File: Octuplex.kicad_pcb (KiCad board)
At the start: 2 copper layers, 140 x 140 mm, 21 parts, among them U1 MC68B09, U11 74LS138, U2 MC68B40, U3 MC68B50, U4 27128, U5 HM62256BLP, U6 74LS139, U8 74LS259, X1 CXO_DIP8, X2 CXO_DIP8

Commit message: Break up schematic into hierarchial sheets.
Connect sheets with address and data buses. TODO: add control bus.
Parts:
- added C1: 0.1uF, Capacitor_THT:C_Radial_D6.3mm_H5.0mm_P2.50mm, F.Cu at (232.7, 93.0)
- added C2: 0.1uF, Capacitor_THT:C_Radial_D6.3mm_H5.0mm_P2.50mm, F.Cu at (232.7, 100.8)
- U10: value ~ -> R6522
- U3: value MC68B50 -> MXS6551; footprint Package_DIP:DIP-24_W15.24mm -> Package_DIP:DIP-28_W15.24mm
- U7: value ~ -> MC68B50; footprint Package_DIP:DIP-28_W15.24mm -> Package_DIP:DIP-24_W15.24mm
- moved U10 216.8 mm to (231.6, 19.2), turned to 0 degrees
- moved H2 207.3 mm to (234.0, 85.1)
- moved H1 202.2 mm to (234.0, 77.1)
- moved H3 197.3 mm to (241.9, 77.1)
- moved H8 193.4 mm to (257.8, 85.1)
- moved U7 191.7 mm to (268.4, 19.2), turned to 0 degrees
- moved X1 182.6 mm to (209.6, 50.0)
- moved U8 180.8 mm to (268.4, 51.3), turned to 0 degrees
- moved U11 170.7 mm to (218.8, 19.2)
- moved U6 150.5 mm to (207.9, 19.2)
- moved H4 145.8 mm to (241.9, 85.1)
- moved U9 141.6 mm to (189.5, 19.2)
- moved H7 139.8 mm to (257.8, 77.1)
- moved U1 127.8 mm to (171.1, 19.2)
- moved X2 126.2 mm to (251.7, 65.2)
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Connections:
- U1 pad 2: unconnected-(U1-~{NMI}-Pad2) -> /Microprocessor/~{NMI}
- U1 pad 24: unconnected-(U1-D7-Pad24) -> /d7
- U1 pad 25: unconnected-(U1-D6-Pad25) -> /d6
- U1 pad 26: unconnected-(U1-D5-Pad26) -> /d5
- U1 pad 27: unconnected-(U1-D4-Pad27) -> /d4
- U1 pad 28: unconnected-(U1-D3-Pad28) -> /d3
- U1 pad 29: unconnected-(U1-D2-Pad29) -> /d2
- U1 pad 3: /~{IRQ} -> /Microprocessor/~{IRQ}
- U1 pad 30: unconnected-(U1-D1-Pad30) -> /d1
- U1 pad 31: unconnected-(U1-D0-Pad31) -> /d0
- U1 pad 34: /E -> /Microprocessor/E
- U1 pad 37: /~{RESET} -> /Microprocessor/~{RESET}
- U10 pad 1: unconnected-(U10-VSS-Pad1) -> GND
- U10 pad 20: unconnected-(U10-VCC-Pad20) -> VCC
- U10 pad 21: /~{IRQ} -> /GPIO/~{IRQ}
- U10 pad 25: /E -> /GPIO/E
- U10 pad 34: /~{RESET} -> /GPIO/~{RESET}
- U11 pad 16: unconnected-(U11-VCC-Pad16) -> VCC
- U11 pad 8: unconnected-(U11-GND-Pad8) -> GND
- U2 pad 17: /E -> /Microprocessor/E
- U2 pad 8: /~{RESET} -> /Microprocessor/~{RESET}
- U2 pad 9: /~{IRQ} -> /Microprocessor/~{IRQ}
- U3 pad 1: unconnected-(U3-VSS-Pad1) -> GND
- U3 pad 13: unconnected-(U3-R/~{W}-Pad13) -> /a0
- U3 pad 14: unconnected-(U3-E-Pad14) -> /a1
- U3 pad 15: /d7 -> VCC
- U3 pad 16: /d6 -> unconnected-(U3-~{DCD}-Pad16)
- U3 pad 17: /d5 -> unconnected-(U3-~{DSR}-Pad17)
- U3 pad 18: /d4 -> /d0
- U3 pad 19: /d3 -> /d1
- U3 pad 21: /d1 -> /d3
- U3 pad 22: /d0 -> /d4
- U3 pad 23: unconnected-(U3-~{DCD}-Pad23) -> /d5
- U3 pad 24: unconnected-(U3-~{CTS}-Pad24) -> /d6
- U3 pad 4: unconnected-(U3-Tx_CLK-Pad4) -> /GPIO/~{RESET}
- U3 pad 7: /~{IRQ} -> unconnected-(U3-XTAL2-Pad7)
- U4 pad 22: unconnected-(U4-~{OE}-Pad22) -> /Microprocessor/E
- U7 pad 11: unconnected-(U7-~{DTR}-Pad11) -> /a0
- U7 pad 12: unconnected-(U7-Rx_Data-Pad12) -> VCC
- U7 pad 14: unconnected-(U7-RS1-Pad14) -> /GPIO/E
- U7 pad 15: VCC -> /d7
- U7 pad 16: unconnected-(U7-~{DCD}-Pad16) -> /d6
- U7 pad 17: unconnected-(U7-~{DSR}-Pad17) -> /d5
- U7 pad 18: /d0 -> /d4
- U7 pad 19: /d1 -> /d3
- U7 pad 21: /d3 -> /d1
- U7 pad 22: /d4 -> /d0
- U7 pad 23: /d5 -> unconnected-(U7-~{DCD}-Pad23)
- U7 pad 24: /d6 -> unconnected-(U7-~{CTS}-Pad24)
- U7 pad 4: /~{RESET} -> unconnected-(U7-Tx_CLK-Pad4)
- U7 pad 7: unconnected-(U7-XTAL2-Pad7) -> /GPIO/~{IRQ}
- U8 pad 15: /~{RESET} -> /GPIO/~{RESET}
- U8 pad 16: unconnected-(U8-VCC-Pad16) -> VCC
- U8 pad 8: unconnected-(U8-GND-Pad8) -> GND
- U9 pad 39: /E -> /Microprocessor/E
- U9 pad 4: /~{IRQ} -> /Microprocessor/~{IRQ}
- U9 pad 40: /~{RESET} -> /Microprocessor/~{RESET}
- U9 pad 6: unconnected-(U9-~{NMI}-Pad6) -> /Microprocessor/~{NMI}
- X1 pad 4: unconnected-(X1-GND-Pad4) -> GND
- X1 pad 8: unconnected-(X1-Vcc-Pad8) -> VCC
- X2 pad 4: unconnected-(X2-GND-Pad4) -> GND
- X2 pad 8: unconnected-(X2-Vcc-Pad8) -> VCC

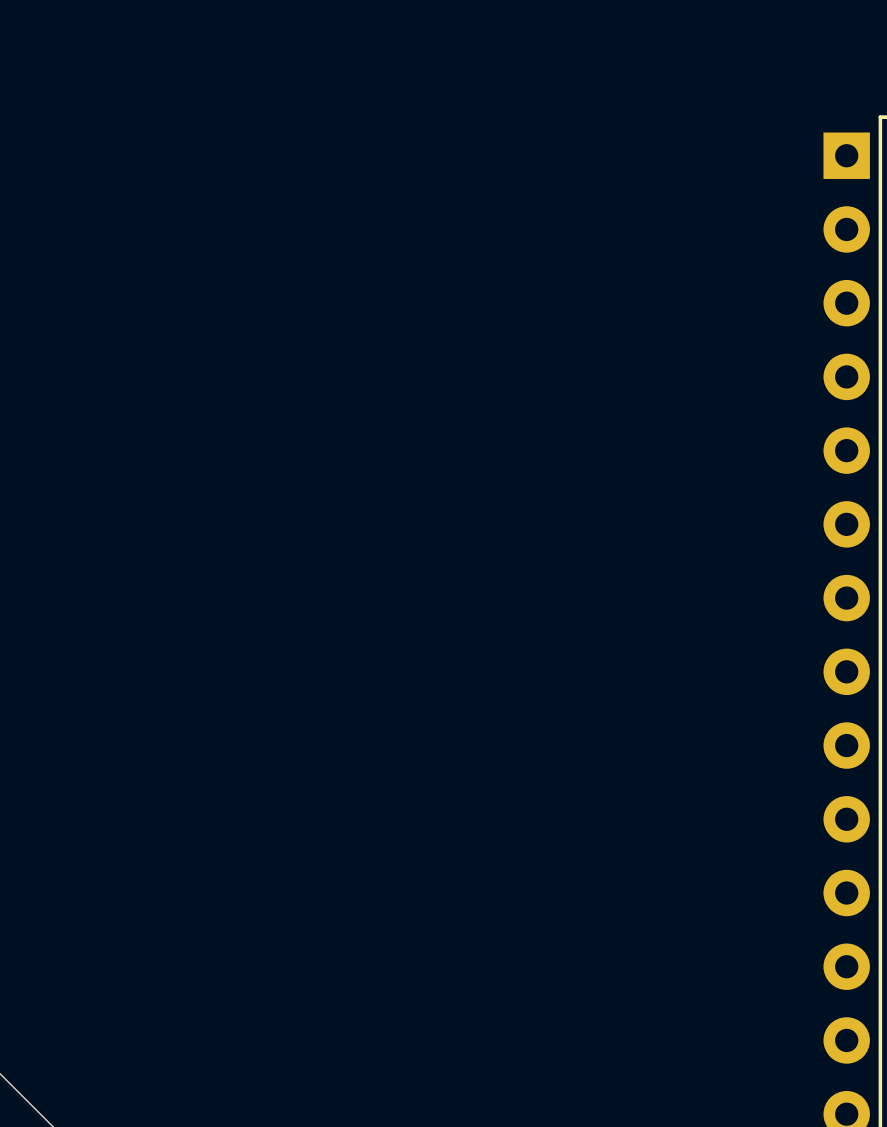
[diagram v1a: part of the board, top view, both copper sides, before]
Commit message: Update schematic.
Pull-up resistors for 6809 signals. 74LS251 mux for 8 input pins. MIDI optoisolator. Wire up 74LS139 for RD and WR. Still many unconnected pins. TODO: connect sheets with control bus.
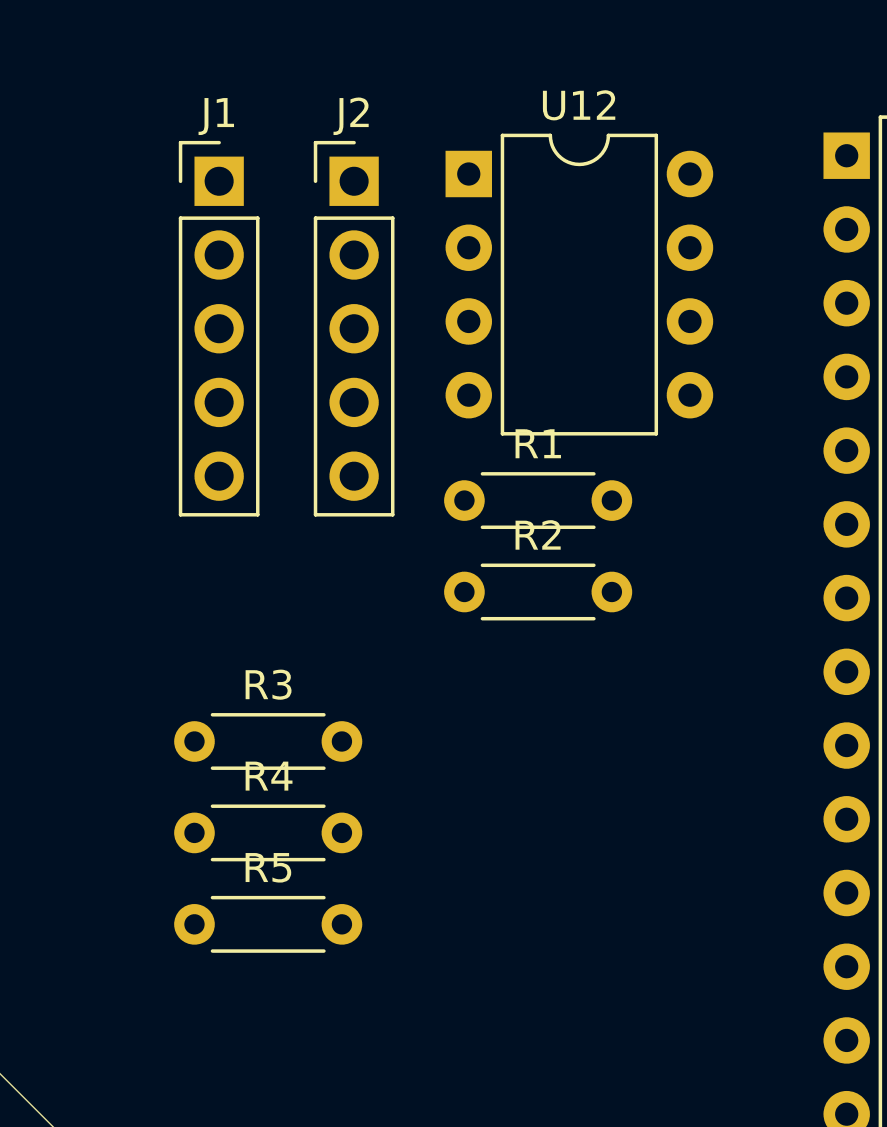
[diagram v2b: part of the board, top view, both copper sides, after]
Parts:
- added J1: DIN-5_180degree, Connector_PinHeader_2.54mm:PinHeader_1x05_P2.54mm_Vertical, F.Cu at (149.4, 20.1)
- added J2: DIN-5_180degree, Connector_PinHeader_2.54mm:PinHeader_1x05_P2.54mm_Vertical, F.Cu at (154.1, 20.1)
- added R1: 220, Resistor_THT:R_Axial_DIN0204_L3.6mm_D1.6mm_P5.08mm_Horizontal, F.Cu at (157.9, 31.1)
- added R2: 280, Resistor_THT:R_Axial_DIN0204_L3.6mm_D1.6mm_P5.08mm_Horizontal, F.Cu at (157.9, 34.3)
- added R3: R, Resistor_THT:R_Axial_DIN0204_L3.6mm_D1.6mm_P5.08mm_Horizontal, F.Cu at (148.6, 39.4)
- added R4: R, Resistor_THT:R_Axial_DIN0204_L3.6mm_D1.6mm_P5.08mm_Horizontal, F.Cu at (148.6, 42.6)
- added R5: R, Resistor_THT:R_Axial_DIN0204_L3.6mm_D1.6mm_P5.08mm_Horizontal, F.Cu at (148.6, 45.7)
- added U12: HCPL-2631, Package_DIP:DIP-8_W7.62mm, F.Cu at (158.0, 19.9)
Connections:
- U1 pad 4: unconnected-(U1-~{FIRQ}-Pad4) -> /Microprocessor/FIRQ
- U10 pad 22: unconnected-(U10-R/~{W}-Pad22) -> /GPIO/R/~{W}
- U10 pad 23: unconnected-(U10-~{CS2}-Pad23) -> /GPIO/~{VIACS}
- U10 pad 24: unconnected-(U10-CS1-Pad24) -> VCC
- U3 pad 28: unconnected-(U3-R/~{W}-Pad28) -> /GPIO/R/~{W}
- U7 pad 10: unconnected-(U7-CS1-Pad10) -> VCC
- U7 pad 2: unconnected-(U7-Rx_Data-Pad2) -> Net-(U12-VO1)
- U7 pad 8: unconnected-(U7-CS0-Pad8) -> VCC
- U7 pad 9: unconnected-(U7-CS2-Pad9) -> /GPIO/~{MIDICS}

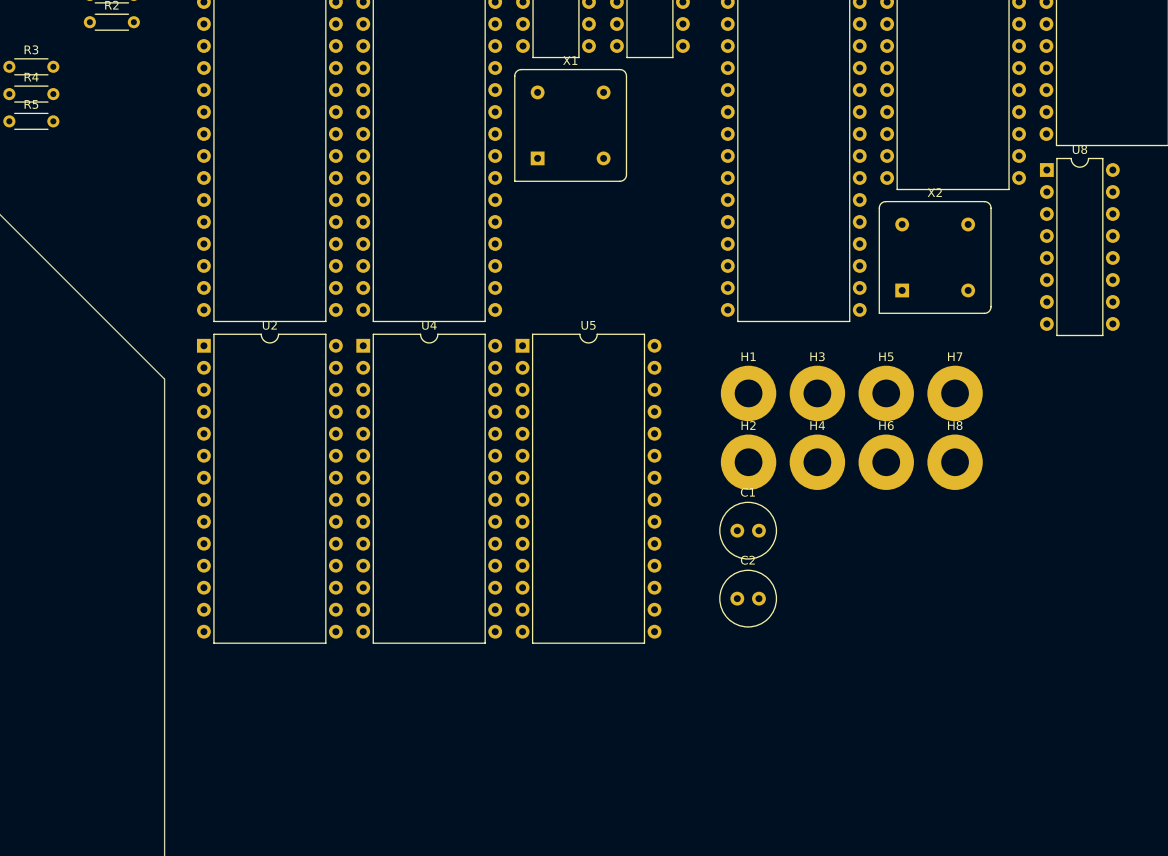
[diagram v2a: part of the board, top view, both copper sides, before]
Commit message: Add control bus.
R/W, E, RD, WR signals from microprocessor to GPIO.
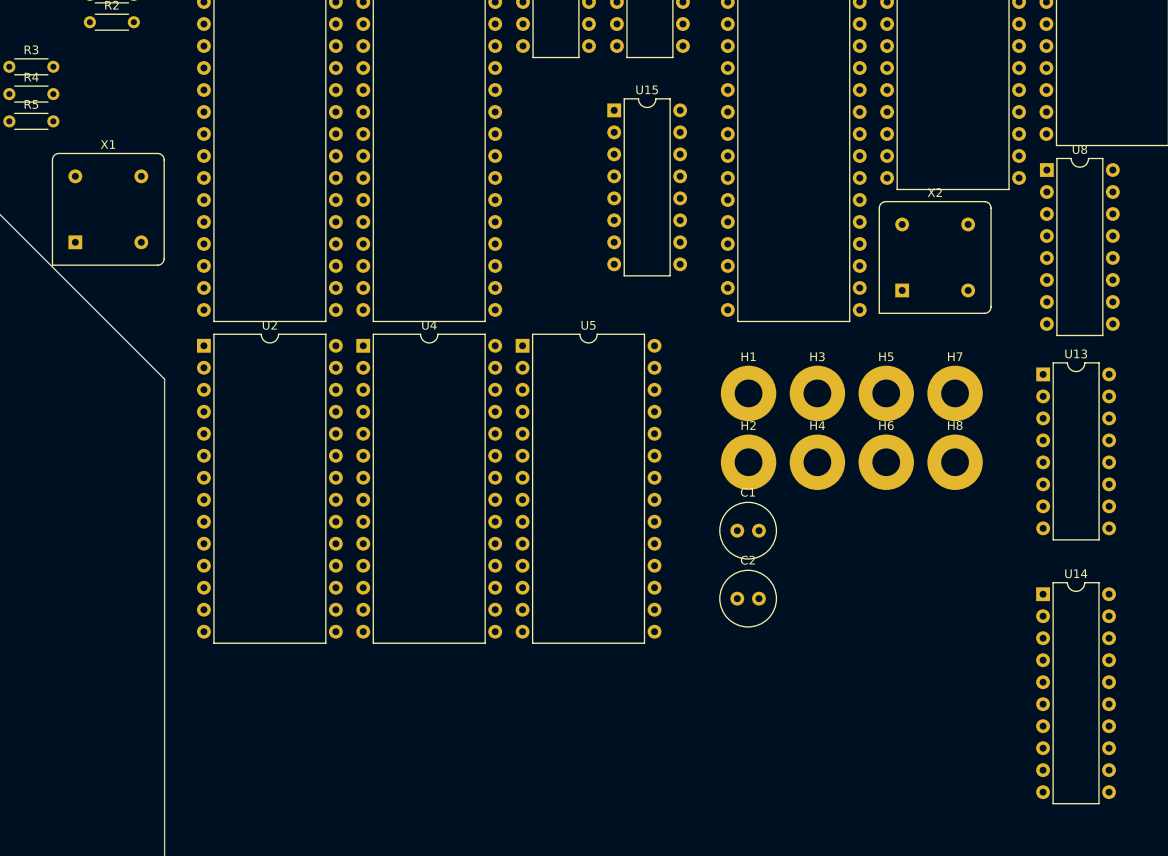
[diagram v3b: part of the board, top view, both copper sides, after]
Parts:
- added U13: 74LS251, Package_DIP:DIP-16_W7.62mm, F.Cu at (268.0, 74.9)
- added U14: PCF8584, Package_DIP:DIP-20_W7.62mm, F.Cu at (268.0, 100.3)
- added U15: 74LS138, Package_DIP:DIP-16_W7.62mm, F.Cu at (218.4, 44.5)
- moved X1 54.3 mm to (156.2, 59.7)
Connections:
- U1 pad 2: /Microprocessor/~{NMI} -> /~{NMI}
- U1 pad 3: /Microprocessor/~{IRQ} -> /~{IRQ}
- U1 pad 32: unconnected-(U1-R/~{W}-Pad32) -> /R/~{W}
- U1 pad 33: unconnected-(U1-~{DMA/BREQ}-Pad33) -> Net-(U1-~{DMA/BREQ})
- U1 pad 34: /Microprocessor/E -> /E
- U1 pad 36: unconnected-(U1-MRDY-Pad36) -> Net-(U1-MRDY)
- U1 pad 37: /Microprocessor/~{RESET} -> /~{RESET}
- U1 pad 38: unconnected-(U1-EXTAL-Pad38) -> Net-(U1-EXTAL)
- U1 pad 4: /Microprocessor/FIRQ -> /~{FIRQ}
- U1 pad 40: unconnected-(U1-~{HALT}-Pad40) -> Net-(U1-~{HALT})
- U10 pad 21: /GPIO/~{IRQ} -> /~{IRQ}
- U10 pad 22: /GPIO/R/~{W} -> /R/~{W}
- U10 pad 25: /GPIO/E -> /E
- U10 pad 34: /GPIO/~{RESET} -> /~{RESET}
- U11 pad 1: unconnected-(U11-A0-Pad1) -> /R/~{W}
- U11 pad 2: unconnected-(U11-A1-Pad2) -> /a11
- U11 pad 3: unconnected-(U11-A2-Pad3) -> /a12
- U11 pad 4: unconnected-(U11-E1-Pad4) -> /Microprocessor/~{IOSEL}
- U11 pad 5: unconnected-(U11-E2-Pad5) -> /a13
- U11 pad 6: /a15 -> /E
- U2 pad 13: unconnected-(U2-R/~{W}-Pad13) -> /R/~{W}
- U2 pad 15: unconnected-(U2-~{CS0}-Pad15) -> /Microprocessor/~{TIMERCS}
- U2 pad 16: unconnected-(U2-CS1-Pad16) -> VCC
- U2 pad 17: /Microprocessor/E -> /E
- U2 pad 8: /Microprocessor/~{RESET} -> /~{RESET}
- U2 pad 9: /Microprocessor/~{IRQ} -> /~{IRQ}
- U3 pad 26: /GPIO/~{IRQ} -> /~{IRQ}
- U3 pad 27: /GPIO/E -> /E
- U3 pad 28: /GPIO/R/~{W} -> /R/~{W}
- U3 pad 4: /GPIO/~{RESET} -> /~{RESET}
- U4 pad 20: unconnected-(U4-~{CE}-Pad20) -> /Microprocessor/~{ROMCS}
- U4 pad 22: /Microprocessor/E -> /~{RD}
- U5 pad 20: unconnected-(U5-~{CS}-Pad20) -> /a15
- U5 pad 22: unconnected-(U5-~{OE}-Pad22) -> /~{RD}
- U5 pad 27: unconnected-(U5-~{WE}-Pad27) -> /~{WR}
- U6 pad 10: unconnected-(U6B-O2-Pad10) -> /Microprocessor/~{IOSEL}
- U6 pad 13: unconnected-(U6B-A1-Pad13) -> /a15
- U6 pad 14: unconnected-(U6B-A0-Pad14) -> /a14
- U6 pad 15: unconnected-(U6B-E-Pad15) -> GND
- U6 pad 2: unconnected-(U6A-A0-Pad2) -> /R/~{W}
- U6 pad 3: unconnected-(U6A-A1-Pad3) -> /E
- U6 pad 6: unconnected-(U6A-O2-Pad6) -> /~{WR}
- U6 pad 7: unconnected-(U6A-O3-Pad7) -> /~{RD}
- U6 pad 9: unconnected-(U6B-O3-Pad9) -> /Microprocessor/~{ROMCS}
- U7 pad 13: unconnected-(U7-R/~{W}-Pad13) -> /R/~{W}
- U7 pad 14: /GPIO/E -> /E
- U7 pad 7: /GPIO/~{IRQ} -> /~{IRQ}
- U8 pad 14: unconnected-(U8-E-Pad14) -> /~{WR}
- U8 pad 15: /GPIO/~{RESET} -> /~{RESET}
- U9 pad 34: unconnected-(U9-R/~{W}-Pad34) -> /R/~{W}
- U9 pad 39: /Microprocessor/E -> /E
- U9 pad 4: /Microprocessor/~{IRQ} -> /~{IRQ}
- U9 pad 40: /Microprocessor/~{RESET} -> /~{RESET}
- U9 pad 6: /Microprocessor/~{NMI} -> /~{NMI}
- X1 pad 5: unconnected-(X1-OUT-Pad5) -> Net-(U1-EXTAL)

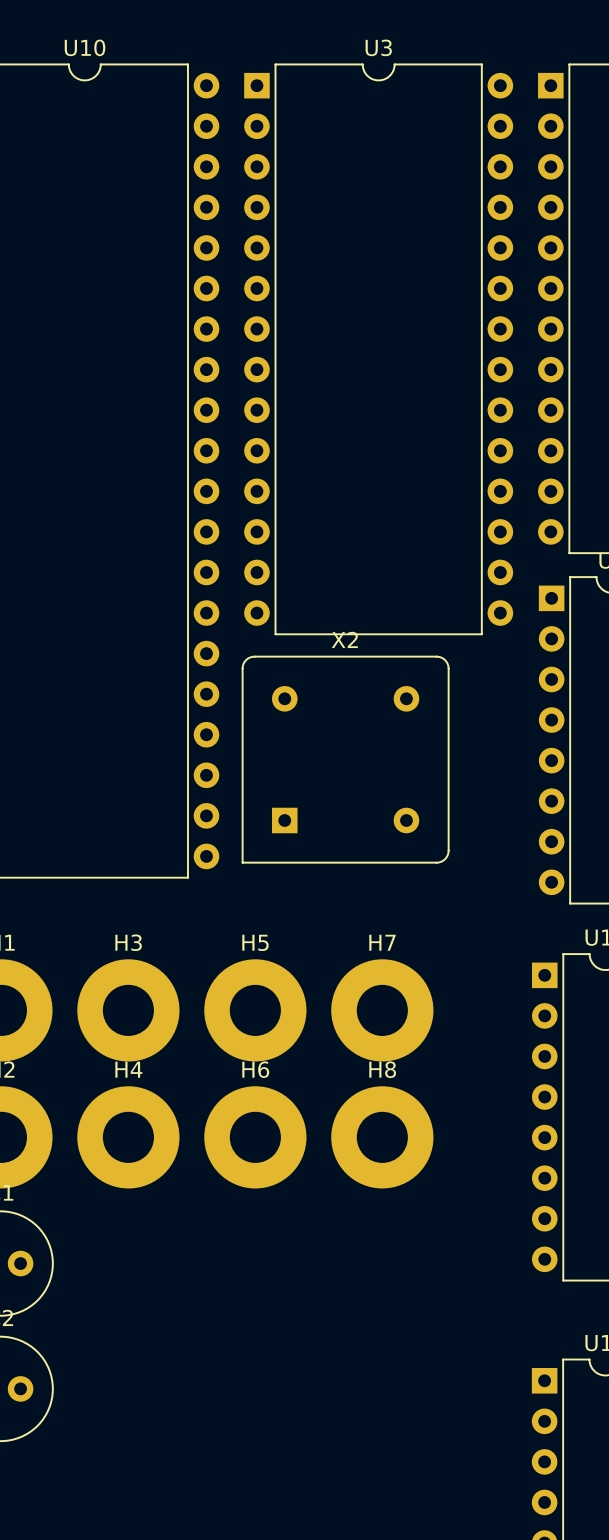
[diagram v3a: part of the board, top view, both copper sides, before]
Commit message: Replace 6551 with R65C52 (dual ACIA).
New symbol for R65C52 in library. Two async serial ports in one 40-pin package. But it has no 'E' input. Also remove two misconnected WR and RD pins.
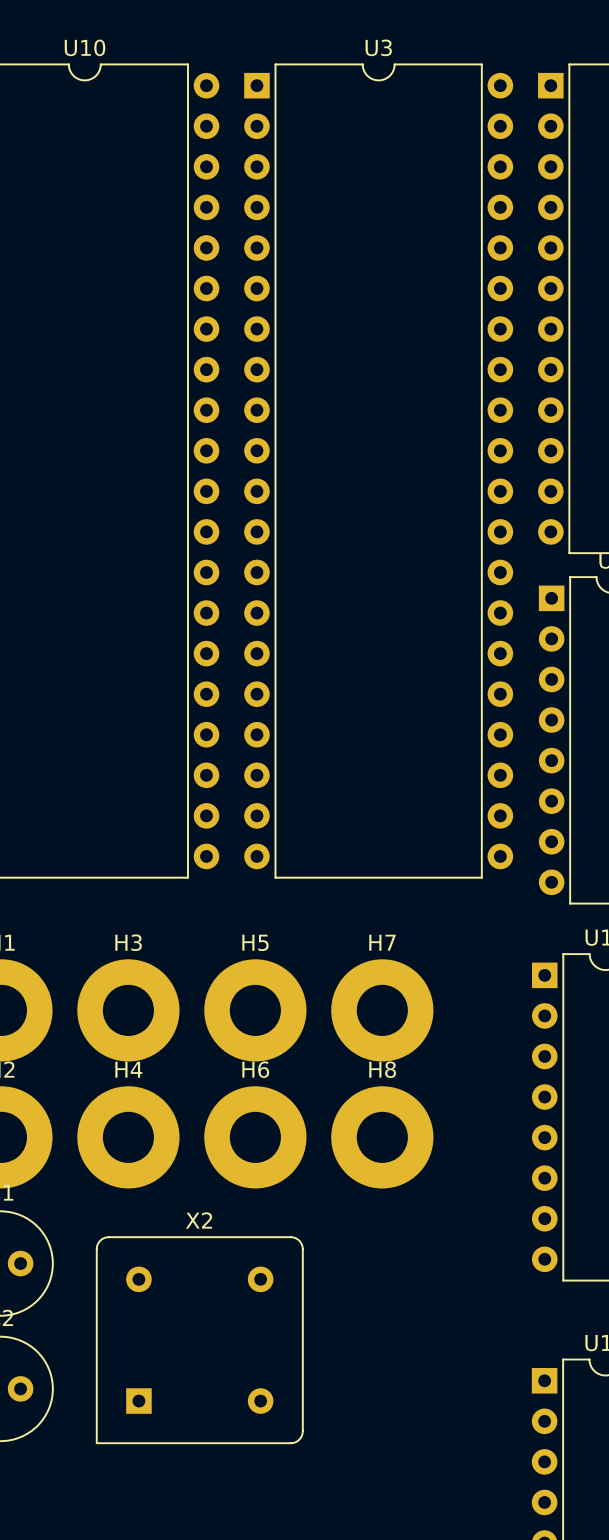
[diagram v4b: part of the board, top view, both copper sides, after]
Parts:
- R3, R4, R5: value R -> 10k
- U3: value MXS6551 -> R65C52; footprint Package_DIP:DIP-28_W15.24mm -> Package_DIP:DIP-40_W15.24mm
- U9: value ~ -> M6502
- moved X2 37.5 mm to (242.6, 101.6)
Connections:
- R3 pad 2: /Microprocessor/~{NMI} -> /~{RESET}
- R4 pad 2: /Microprocessor/~{IRQ} -> Net-(U1-MRDY)
- R5 pad 2: /Microprocessor/FIRQ -> Net-(U1-~{HALT})
- U13 pad 7: /~{RD} -> unconnected-(U13-~{OE}-Pad7)
- U3 pad 1: GND -> /~{RESET}
- U3 pad 11: unconnected-(U3-~{DTR}-Pad11) -> /~{IRQ}
- U3 pad 13: /a0 -> unconnected-(U3-~{DTR2}-Pad13)
- U3 pad 14: /a1 -> unconnected-(U3-TxD2-Pad14)
- U3 pad 15: VCC -> unconnected-(U3-TxC-Pad15)
- U3 pad 16: unconnected-(U3-~{DCD}-Pad16) -> /d7
- U3 pad 17: unconnected-(U3-~{DSR}-Pad17) -> /d6
- U3 pad 18: /d0 -> /d5
- U3 pad 19: /d1 -> /d4
- U3 pad 20: /d2 -> GND
- U3 pad 22: /d4 -> /d2
- U3 pad 23: /d5 -> /d1
- U3 pad 24: /d6 -> /d0
- U3 pad 25: /d7 -> unconnected-(U3-RxC-Pad25)
- U3 pad 26: /~{IRQ} -> unconnected-(U3-TxD1-Pad26)
- U3 pad 27: /E -> unconnected-(U3-~{DTR1}-Pad27)
- U3 pad 28: /R/~{W} -> unconnected-(U3-RxD1-Pad28)
- U3 pad 4: /~{RESET} -> unconnected-(U3-XTALO-Pad4)
- U8 pad 14: /~{WR} -> unconnected-(U8-E-Pad14)
